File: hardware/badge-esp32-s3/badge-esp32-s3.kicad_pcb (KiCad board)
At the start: 2 copper layers, 131.5 x 83.5 mm, 122 parts, among them J1 Connector, USB-TYPE-C-16P, J2 Connector, USB-TYPE-C-16P, P1 PH-2A_C2319, Q1 SS8050 200-350, Q2 SS8050 200-350, Q3 HL2301A, SW3 SK-12F04-G050, SW4 TS665CJ, SW5 TS665CJ, SW6 TS665CJ, SW7 TS665CJ, SW8 TS665CJ, SW9 TS665CJ, U1 ESP32-S3-MINI-1-N8, U10 FH2.54-09-02PZD, U11 FH2.54-09-04PZD, U12 FH2.54-09-03PZD, U13 FH2.54-09-02PZD, U14 FH2.54-09-04PZD, U15 FH2.54-09-04PZD, U16 FH2.54-09-04PZD, U17 FH2.54-09-02PZD, U18 MMA8452QR1_C11360, U19 FH2.54-09-02PZD, U2 NCP167BMX330TBG, U3 CP2102N-A02-GQFN28R, U4 TP4056, U5 FH2.54-09-02PZD, U7 FH2.54-09-02PZD, U8 FH2.54-09-03PZD, U9 FH2.54-09-03PZD

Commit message: Finish beta layout for ordering
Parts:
- moved G*** 24.7 mm to (198.5, 103.0)
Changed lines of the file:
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@@
 	(footprint "misc-lib:QRCodeFootPrint"
 		(layer "B.Cu")
-		(at 201.5 78.5 180)
+		(at 198.5 103 180)
 		(property "Reference" "G***"
 			(at 0 0 0)
@@
 	)
 	(gr_text "Protocols"
-		(at 129 82 0)
+		(at 128.5 85.5 0)
 		(layer "B.SilkS")
 		(effects
@@
 	)
 	(gr_text "Display\n	Reset: 48\n	Data/Command: 37\n	(See SPI pins)\n\nMinibadge\n	CLK: 12\n	(See I2C)\n\nJoystick (Optional)\n	X axis: 1\n	Y axis: 2"
-		(at 166.5 126.5 0)
+		(at 164.5 124.5 0)
 		(layer "B.SilkS")
 		(effects
 			(font
-				(size 2 2)
+				(size 1.7 1.7)
 				(thickness 0.15)
 			)
@@
 	)
 	(gr_text "UART\n	TX: 43\n	RX: 44\n\nSPI\n	CLK: 32\n	MOSI: 31\n	MISO: 29\n	SD CS: 26\n	Display CS: 33\n\nI2C\n	SCL: 21\n	SDA: 47"
-		(at 131 133.5 0)
+		(at 126.5 127.5 0)
 		(layer "B.SilkS")
 		(effects
 			(font
-				(size 2 2)
+				(size 1.7 1.7)
 				(thickness 0.15)
 			)
@@
 	)
 	(gr_text "Peripherals"
-		(at 185 82 0)
+		(at 179 86 0)
 		(layer "B.SilkS")
 		(effects
@@
 	)
 	(gr_text "LED: 41\nBuzzer: 42\n\nRGB LED\n	Red: 38\n	Green: 39\n	Blue: 40\n\nButtons\n	Right: 13\n	Left: 14\n	Down: 15\n	Up: 16\n	B: 17\n	A: 18"
-		(at 192.5 130.5 0)
+		(at 185.5 130 0)
 		(layer "B.SilkS")
 		(effects
 			(font
-				(size 2 2)
-				(thickness 0.15)
-			)
+				(size 1.7 1.7)
+				(thickness 0.15)
+			)

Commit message: Oopsies, forgot to push my changes for final production (Spring 2025)
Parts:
- U1: footprint RF_Module:ESP32-S2-MINI-1 -> lcsc-lib:ESP32-S3-MINI-1
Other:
- outline, holes or cut-outs redrawn
- board text added: "Display Reset: 48 Data/Command: 37 (See SPI pins) Minibadge CLK: 12 (See I2C) Joystick (Optional) X axis: 1 Y axis: 2 Accelerometer Address: 0x1C"
- board text added: "Name:"
- board text removed: "Display Reset: 48 Data/Command: 37 (See SPI pins) Minibadge CLK: 12 (See I2C) Joystick (Optional) X axis: 1 Y axis: 2"
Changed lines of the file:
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@@
 		)
 	)
-	(footprint "RF_Module:ESP32-S2-MINI-1"
+	(footprint "lcsc-lib:ESP32-S3-MINI-1"
 		(layer "F.Cu")
 		(at 150.65 75.45)
@@
 			)
 		)
-		(property "Datasheet" "https://www.espressif.com/sites/default/files/documentation/esp32-s3-mini-1_mini-1u_datasheet_en.pdf"
+		(property "Datasheet" ""
 			(at 0 0 0)
 			(unlocked yes)
@@
 			)
 		)
-		(property "Description" "RF Module, ESP32-S3 SoC, Wi-Fi 802.11b/g/n, Bluetooth, BLE, 32-bit, 3.3V, SMD, onboard antenna"
+		(property "Description" ""
 			(at 0 0 0)
 			(unlocked yes)
@@
 			)
 		)
+		(model "/home/carson/e-badge/hardware/lcsc-lib/lcsc-lib.3dshapes/BULETM-SMD_ESP32-S3-MINI-1-N8.wrl"
+			(offset
+				(xyz 0 0 0)
+			)
+			(scale
+				(xyz 1 1 1)
+			)
+			(rotate
+				(xyz 0 0 0)
+			)
+		)
 	)
 	(footprint "PCM_JLCPCB:R_0603"
@@
 		(model "/home/carson/e-badge/hardware/lcsc-lib/lcsc-lib.3dshapes/SW-TH_G-SWITCH_SK-12F04-G050.wrl"
 			(offset
-				(xyz 0 -2.5 0)
+				(xyz 0 0 4.5)
 			)
 			(scale
@@
 			)
 			(rotate
-				(xyz 0 0 0)
+				(xyz -0 -0 -0)
 			)
 		)
@@
 			(layer "F.Fab")
 		)
+		(fp_text user "${REFERENCE}"
+			(at 0 0 90)
+			(layer "F.Fab")
+			(effects
+				(font
+					(size 1 1)
+					(thickness 0.15)
+				)
+			)
+		)
 		(pad "1" smd rect
 			(at -0.75 0 90)
@@
 			(pinfunction "SHIELD")
 			(pintype "passive")
-			(zone_connect 1)
 		)
 		(pad "S1" thru_hole oval
@@
 			(layer "F.Fab")
 		)
+		(fp_text user "${REFERENCE}"
+			(at 0 0 0)
+			(layer "F.Fab")
+			(effects
+				(font
+					(size 1 1)
+					(thickness 0.15)
+				)
+			)
+		)
 		(pad "1" smd rect
 			(at -0.75 0)
@@
 		(model "/home/carson/e-badge/hardware/lcsc-lib/lcsc-lib.3dshapes/HDR2.54-F-LI-1X3P.wrl"
 			(offset
-				(xyz 0 -0 0)
+				(xyz 2.5 0 0)
 			)
 			(scale
@@
 			)
 			(rotate
-				(xyz 0 0 0)
+				(xyz -0 -0 -0)
 			)
 		)
@@
 		)
 		(fp_line
-			(start -3.5 -2.5)
-			(end 3 -2.5)
-			(stroke
-				(width 0.1)
-				(type default)
-			)
-			(layer "F.SilkS")
-		)
-		(fp_line
 			(start -11.69 -5.25)
 			(end -11.69 -18.2)
@@
 			)
 		)
+		(pad "1" smd rect
+			(at -2.75 0 270)
+			(size 0.3 5)
+			(layers "F.Cu" "F.Mask" "F.Paste")
+		)
+		(pad "2" smd rect
+			(at -2.25 0 270)
+			(size 0.3 5)
+			(layers "F.Cu" "F.Mask" "F.Paste")
+		)
+		(pad "3" smd rect
+			(at -1.75 0 270)
+			(size 0.3 5)
+			(layers "F.Cu" "F.Mask" "F.Paste")
+		)
+		(pad "4" smd rect
+			(at -1.25 0 270)
+			(size 0.3 5)
+			(layers "F.Cu" "F.Mask" "F.Paste")
+		)
+		(pad "5" smd rect
+			(at -0.75 0 270)
+			(size 0.3 5)
+			(layers "F.Cu" "F.Mask" "F.Paste")
+		)
+		(pad "6" smd rect
+			(at -0.25 0 270)
+			(size 0.3 5)
+			(layers "F.Cu" "F.Mask" "F.Paste")
+		)
+		(pad "7" smd rect
+			(at 0.25 0 270)
+			(size 0.3 5)
+			(layers "F.Cu" "F.Mask" "F.Paste")
+		)
+		(pad "8" smd rect
+			(at 0.75 0 270)
+			(size 0.3 5)
+			(layers "F.Cu" "F.Mask" "F.Paste")
+		)
+		(pad "9" smd rect
+			(at 1.25 0 270)
+			(size 0.3 5)
+			(layers "F.Cu" "F.Mask" "F.Paste")
+		)
+		(pad "10" smd rect
+			(at 1.75 0 270)
+			(size 0.3 5)
+			(layers "F.Cu" "F.Mask" "F.Paste")
+		)
+		(pad "11" smd rect
+			(at 2.25 0 270)
+			(size 0.3 5)
+			(layers "F.Cu" "F.Mask" "F.Paste")
+		)
+		(pad "12" smd rect
+			(at 2.75 0 270)
+			(size 0.3 5)
+			(layers "F.Cu" "F.Mask" "F.Paste")
+		)
 		(embedded_fonts no)
 	)
@@
 		(model "/home/carson/e-badge/hardware/lcsc-lib/lcsc-lib.3dshapes/HDR2.54-F-LI-1X3P.wrl"
 			(offset
-				(xyz 0 -0 0)
+				(xyz 2.5 0 0)
 			)
 			(scale
@@
 			)
 			(rotate
-				(xyz 0 0 0)
+				(xyz -0 -0 -0)
 			)
 		)
@@
 			(layer "F.Fab")
 		)
+		(fp_text user "${REFERENCE}"
+			(at 0 0 90)
+			(layer "F.Fab")
+			(effects
+				(font
+					(size 1 1)
+					(thickness 0.15)
+				)
+			)
+		)
 		(pad "1" smd rect
 			(at -0.75 0 90)
@@
 		(model "/home/carson/e-badge/hardware/lcsc-lib/lcsc-lib.3dshapes/HDR2.54-F-LI-1X3P.wrl"
 			(offset
-				(xyz 0 -0 0)
+				(xyz 2.5 0 0)
 			)
 			(scale
@@
 			)
 			(rotate
-				(xyz 0 0 0)
+				(xyz -0 -0 -0)
 			)
 		)
@@
 			(layer "F.Fab")
 		)
+		(fp_text user "${REFERENCE}"
+			(at 0 0 0)
+			(layer "F.Fab")
+			(effects
+				(font
+					(size 1 1)
+					(thickness 0.15)
+				)
+			)
+		)
 		(pad "1" smd rect
 			(at -0.75 0)
@@
 			(layer "F.Fab")
 		)
+		(fp_text user "${REFERENCE}"
+			(at 0 0 0)
+			(layer "F.Fab")
+			(effects
+				(font
+					(size 1 1)
+					(thickness 0.15)
+				)
+			)
+		)
 		(pad "1" smd rect
 			(at -0.75 0)
@@
 			(layer "F.Fab")
 		)
+		(fp_text user "${REFERENCE}"
+			(at 0 0 90)
+			(layer "F.Fab")
+			(effects
+				(font
+					(size 1 1)
+					(thickness 0.15)
+				)
+			)
+		)
 		(pad "1" smd rect
 			(at -0.75 0 90)
@@
 	)
 	(gr_rect
+		(start 86.3875 71.2475)
+		(end 130.6125 79.7525)
+		(stroke
+			(width 0.1)
+			(type solid)
+		)
+		(fill yes)
+		(layer "B.SilkS")
+	)
+	(gr_rect
+		(start 160.5 64.5)
+		(end 172 67.5)
+		(stroke
+			(width 0.05)
+			(type default)
+		)
+		(fill no)
+		(layer "Edge.Cuts")
+	)
+	(gr_rect
 		(start 83.5 63)
 		(end 215 146.5)
@@
 		(layer "Edge.Cuts")
 	)
+	(gr_rect
+		(start 129.5 64.5)
+		(end 140.5 67.5)
+		(stroke
+			(width 0.05)
+			(type default)
+		)
+		(fill no)
+		(layer "Edge.Cuts")
+	)
 	(gr_text "TX"
 		(at 172 130 90)
@@
 		)
 	)
-	(gr_text "Display\n	Reset: 48\n	Data/Command: 37\n	(See SPI pins)\n\nMinibadge\n	CLK: 12\n	(See I2C)\n\nJoystick (Optional)\n	X axis: 1\n	Y axis: 2"
-		(at 164.5 124.5 0)
+	(gr_text "Name:"
+		(at 146 76 0)
+		(layer "B.SilkS")
+		(effects
+			(font
+				(size 3 3)
+				(thickness 0.6)
+				(bold yes)
+			)
+			(justify left bottom mirror)
+		)
+	)
+	(gr_text "Display\n	Reset: 48\n	Data/Command: 37\n	(See SPI pins)\n\nMinibadge\n	CLK: 12\n	(See I2C)\n\nJoystick (Optional)\n	X axis: 1\n	Y axis: 2\n\nAccelerometer\n	Address: 0x1C"
+		(at 164.98 130.25 0)
 		(layer "B.SilkS")
 		(effects

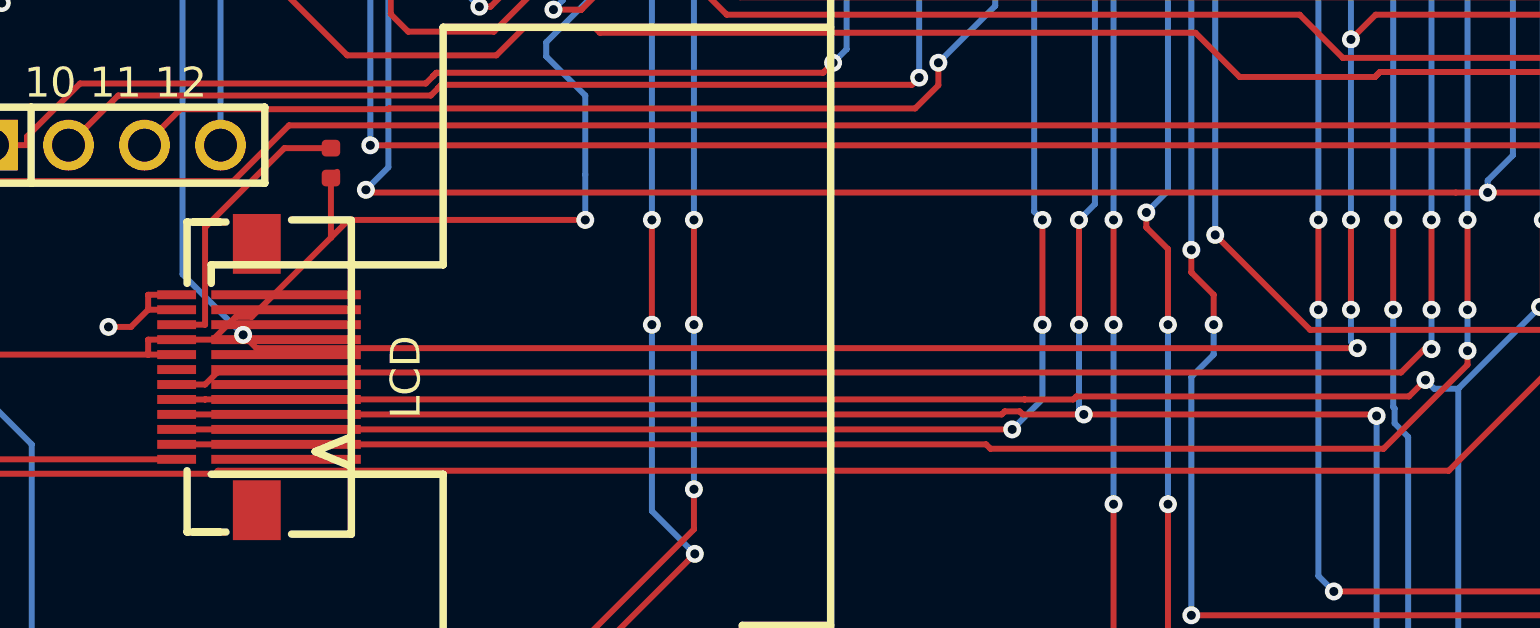
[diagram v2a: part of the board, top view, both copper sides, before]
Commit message: Add comments in PCB editor EXTREMELY SEVERE DRC VIOLATIONS AFTER MERGING
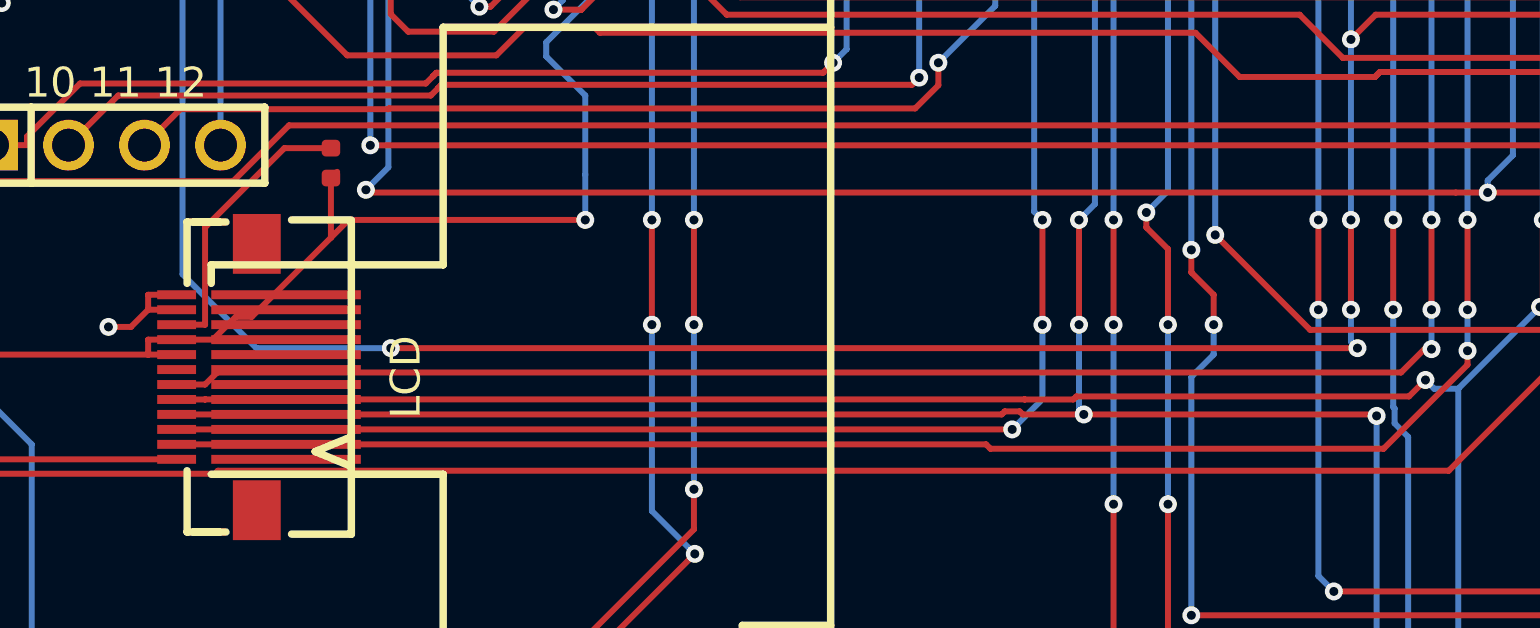
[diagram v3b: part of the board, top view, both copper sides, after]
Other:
- board text added: "<- This is the old connector THERE ARE DRC VIOLATIONS HERE YOU SHOULD FIX"
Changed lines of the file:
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@@
 		)
 	)
+	(gr_text "<- This is the old connector\n	THERE ARE DRC VIOLATIONS HERE YOU SHOULD FIX"
+		(at 120.5 111.5 0)
+		(layer "User.4")
+		(effects
+			(font
+				(size 1 1)
+				(thickness 0.125)
+			)
+			(justify left bottom)
+		)
+	)
 	(segment
 		(start 157.65 78)
@@
 	)
 	(segment
-		(start 116.509 106.284)
-		(end 116.065 105.84)
-		(width 0.2)
-		(layer "F.Cu")
-		(net 28)
-	)
-	(segment
 		(start 166 142.452)
 		(end 166.402 142.853)
@@
 	)
 	(segment
-		(start 153.306 106.284)
-		(end 116.509 106.284)
+		(start 152.35 85)
+		(end 152.35 84.2983)
 		(width 0.2)
 		(layer "F.Cu")
@@
 	)
 	(segment
-		(start 152.35 85)
-		(end 152.35 84.2983)
+		(start 121 106.284)
+		(end 153.306 106.284)
 		(width 0.2)
 		(layer "F.Cu")
@@
 	)
 	(via
-		(at 116.065 105.84)
+		(at 121 106.284)
 		(size 0.6)
 		(drill 0.3)
@@
 	)
 	(segment
-		(start 116.065 105.84)
-		(end 114.04 103.815)
-		(width 0.2)
-		(layer "B.Cu")
-		(net 28)
-	)
-	(segment
 		(start 201.994 97.2765)
 		(end 203.92 95.3506)
@@
 	)
 	(segment
-		(start 114.04 103.815)
-		(end 114.04 87.679)
+		(start 177.54 138)
+		(end 177.54 136.913)
 		(width 0.2)
 		(layer "B.Cu")
@@
 	)
 	(segment
-		(start 177.54 138)
-		(end 177.54 136.913)
+		(start 181.5 116)
+		(end 181.5 113.5)
 		(width 0.2)
 		(layer "B.Cu")
@@
 	)
 	(segment
-		(start 114.04 87.679)
-		(end 111.691 85.3297)
+		(start 181.5 131.5)
+		(end 181.5 127)
 		(width 0.2)
 		(layer "B.Cu")
@@
 	)
 	(segment
-		(start 181.5 116)
-		(end 181.5 113.5)
+		(start 196.744 92.0268)
+		(end 196.744 88.7407)
 		(width 0.2)
 		(layer "B.Cu")
@@
 	)
 	(segment
-		(start 181.5 131.5)
-		(end 181.5 127)
+		(start 116.509 106.284)
+		(end 114.04 103.815)
 		(width 0.2)
 		(layer "B.Cu")
@@
 	)
 	(segment
-		(start 196.744 92.0268)
-		(end 196.744 88.7407)
+		(start 114.04 87.679)
+		(end 111.691 85.3297)
 		(width 0.2)
 		(layer "B.Cu")
@@
 	)
 	(segment
+		(start 121 106.284)
+		(end 116.509 106.284)
+		(width 0.2)
+		(layer "B.Cu")
+		(net 28)
+	)
+	(segment
 		(start 153.088 105)
 		(end 153.088 106.066)
@@
 		(width 0.2)
 		(layer "B.Cu")
+		(net 28)
+	)
+	(segment
+		(start 114.04 103.815)
+		(end 114.04 87.679)
+		(width 0.2)
+		(layer "B.Cu")

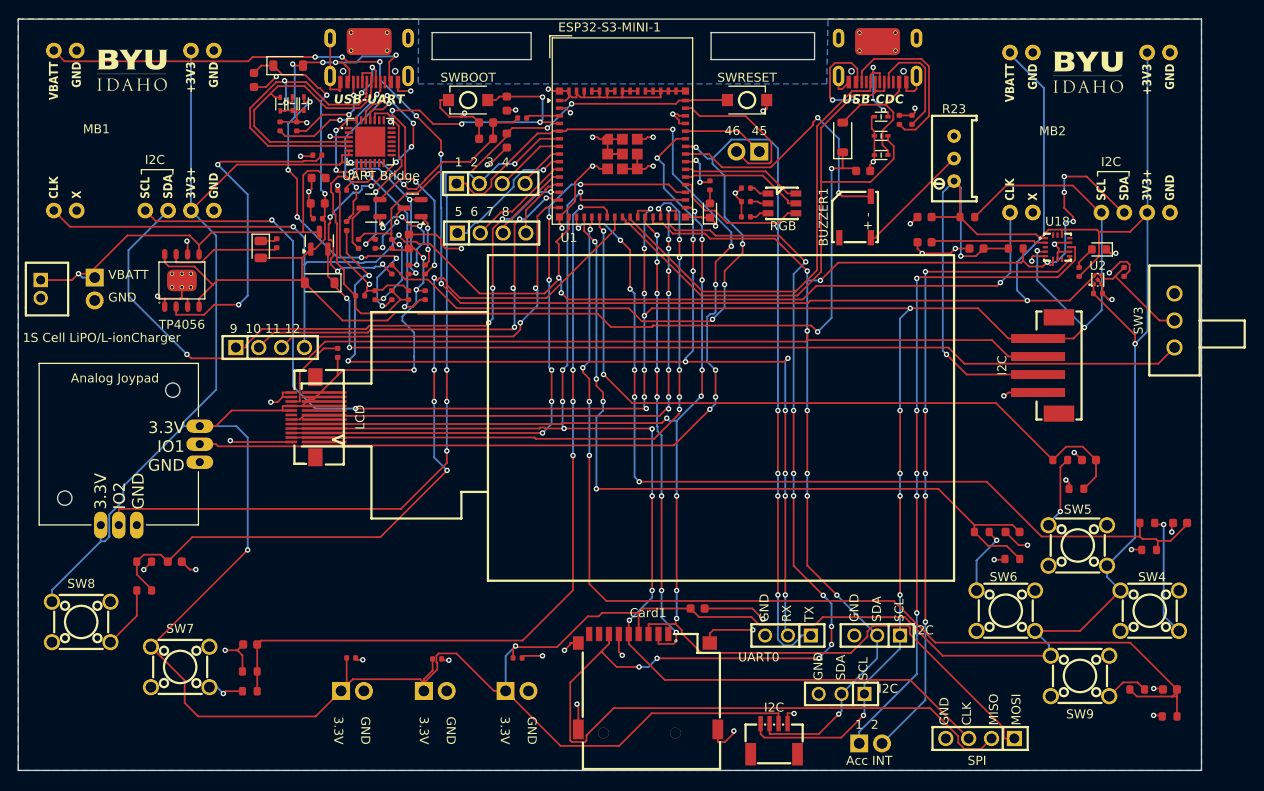
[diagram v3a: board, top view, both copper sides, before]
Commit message: Screen Port Fix
Redo on the screen port fix on the most up-to-date board version.
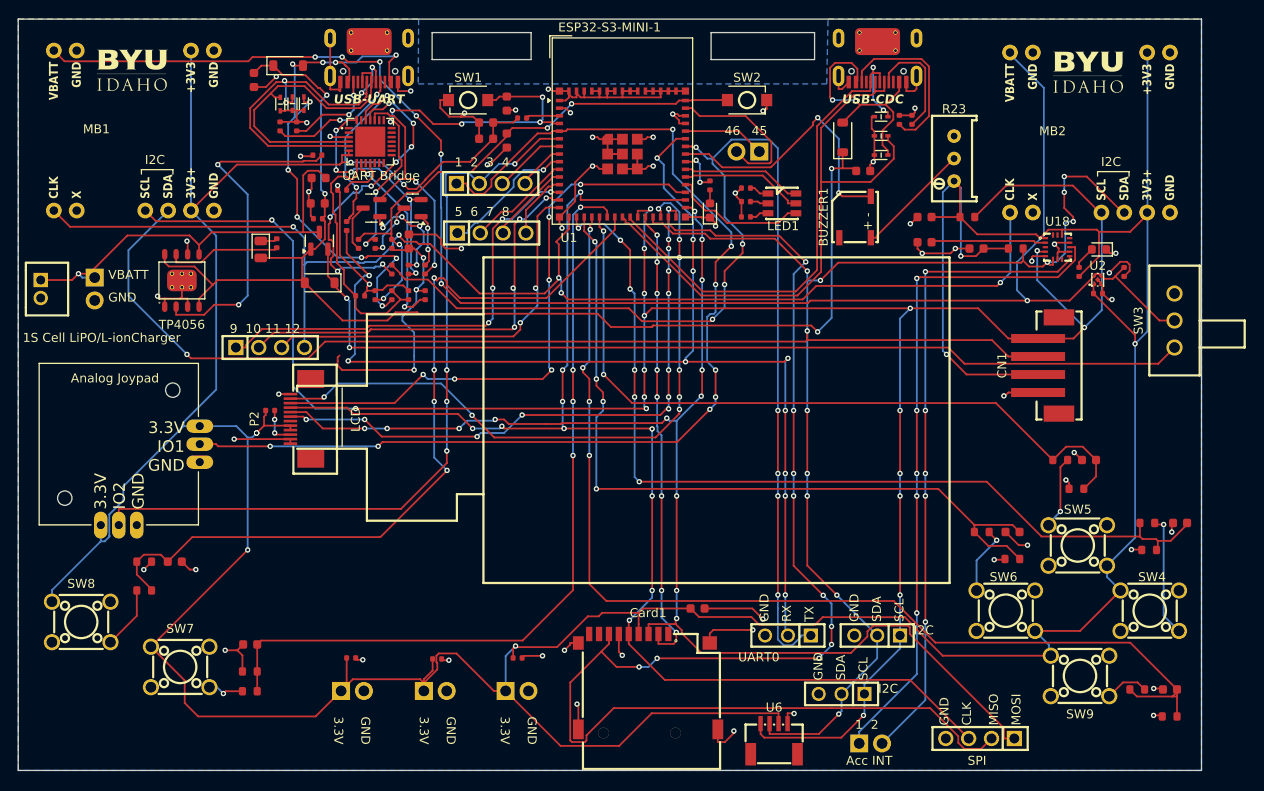
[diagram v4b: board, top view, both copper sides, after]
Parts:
- removed J3: ~, lcsc-lib:FPC-SMD_AFC01-S12FCA-00
- added P2: FPC 0.5MM 12P Pull type H2.0mm Pick up, lcsc-lib:FPC-SMD_12P-L11.5-W5.4-P0.50, F.Cu at (114.9, 107.4)
- U1: footprint lcsc-lib:ESP32-S3-MINI-1 -> RF_Module:ESP32-S2-MINI-1
- moved R18 9.86 mm to (111.5, 106.5), turned to 0 degrees
- moved LCD 0.56 mm to (117.0, 107.5)
- renumbered I2C to CN1, RGB to LED1, SWBOOT to SW1, SWRESET to SW2, I2C to U6
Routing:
- net +3.3V: track 537.9 -> 525.4 mm, vias 10 -> 12
- net Net-(P2-A): track 9.51 -> 4.32 mm, vias 0 -> 2
- net /GPIO37: track 70.1 -> 65.8 mm
- net /GPIO33: track 70.8 -> 74.0 mm, vias 6 -> 8
- net GND: track 250.5 -> 247.7 mm
- net /GPIO48: track 66.3 -> 68.1 mm, vias 8 -> 12
- net /GPIO35: track 143.2 -> 144.7 mm, vias 9 -> 13
- net /GPIO36: track 147.0 -> 148.2 mm, vias 8 -> 10
- net /GPIO1: vias 6 -> 8
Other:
- board text added: "TODO: <- THERE ARE DRC VIOLATIONS HERE"
- board text removed: "<- This is the old connector THERE ARE DRC VIOLATIONS HERE YOU SHOULD FIX"

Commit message: Update badge-esp32-s3.kicad_pcb
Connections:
- Card1 pad CD: (no net) -> unconnected-(Card1-PadCD)
- R27 pad 2: /GPIO13 -> GND
- R28 pad 1: /GPIO13 -> Net-(SW4-D)
- R28 pad 2: GND -> /GPIO13
- R29 pad 2: /GPIO16 -> GND
- R30 pad 1: /GPIO16 -> Net-(SW5-D)
- R30 pad 2: GND -> /GPIO16
- R31 pad 2: /GPIO14 -> GND
- R32 pad 1: /GPIO14 -> Net-(SW6-D)
- R32 pad 2: GND -> /GPIO14
- R33 pad 2: /GPIO17 -> GND
- R34 pad 1: /GPIO17 -> Net-(SW7-D)
- R34 pad 2: GND -> /GPIO17
- R35 pad 2: /GPIO18 -> GND
- R36 pad 1: /GPIO18 -> Net-(SW8-D)
- R36 pad 2: GND -> /GPIO18
- R37 pad 2: /GPIO15 -> GND
- R38 pad 1: /GPIO15 -> Net-(SW9-D)
- R38 pad 2: GND -> /GPIO15
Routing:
- net GND: track 247.7 -> 241.9 mm, vias 59 -> 54
- net /GPIO18: track 91.2 -> 92.4 mm, vias 4 -> 5
- net /GPIO14: track 87.5 -> 88.7 mm, vias 4 -> 5
- net /GPIO13: track 101.7 -> 102.9 mm, vias 6 -> 7
- net /GPIO16: track 81.3 -> 82.5 mm, vias 2 -> 3
- net /GPIO15: track 120.9 -> 121.9 mm, vias 4 -> 5
